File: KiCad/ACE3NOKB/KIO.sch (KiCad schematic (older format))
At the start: 7 parts, among them J100 Conn_02x05_Odd_Even, J101 Conn_02x05_Odd_Even, J102 Conn_02x05_Odd_Even, J103 Conn_02x03_Odd_Even, J104 Conn_02x03_Odd_Even, J105 Conn_02x04_Odd_Even

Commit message: Double check transistors
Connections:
- net ~CPUCLK renamed PHI
- no-connect marks 10 -> 9
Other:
- moved on the sheet: J103, J104, J105
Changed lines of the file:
@@
 	1    0    0    -1
 $EndComp
-NoConn ~ 1350 2850
-NoConn ~ 2575 5950
-Text Label 2475 5650 2    50   ~ 0
+NoConn ~ 2300 5950
+Text Label 2200 5650 2    50   ~ 0
 CLK\TRG0
-Text Label 2475 5750 2    50   ~ 0
+Text Label 2200 5750 2    50   ~ 0
 CLK\TRG1
-Text Label 2475 5850 2    50   ~ 0
+Text Label 2200 5850 2    50   ~ 0
 CLK\TRG2
 $Comp
 L Connector_Generic:Conn_02x04_Odd_Even J105
 U 1 1 6602BBD4
-P 2775 5750
-F 0 "J105" H 2825 6100 50  0000 C CNN
-F 1 "Conn_02x04_Odd_Even" H 2825 6000 50  0000 C CNN
-F 2 "Connector_PinHeader_2.54mm:PinHeader_2x04_P2.54mm_Vertical" H 2775 5750 50  0001 C CNN
-F 3 "~" H 2775 5750 50  0001 C CNN
-	1    2775 5750
+P 2500 5750
+F 0 "J105" H 2550 6100 50  0000 C CNN
+F 1 "Conn_02x04_Odd_Even" H 2550 6000 50  0000 C CNN
+F 2 "Connector_PinHeader_2.54mm:PinHeader_2x04_P2.54mm_Vertical" H 2500 5750 50  0001 C CNN
+F 3 "~" H 2500 5750 50  0001 C CNN
+	1    2500 5750
 	1    0    0    -1
 $EndComp
@@
 L Connector_Generic:Conn_02x03_Odd_Even J104
 U 1 1 64A32B0F
-P 2775 5150
-F 0 "J104" H 2825 5500 50  0000 C CNN
-F 1 "Conn_02x03_Odd_Even" H 2825 5400 50  0000 C CNN
-F 2 "Connector_PinHeader_2.54mm:PinHeader_2x03_P2.54mm_Vertical" H 2775 5150 50  0001 C CNN
-F 3 "~" H 2775 5150 50  0001 C CNN
-	1    2775 5150
+P 2500 5150
+F 0 "J104" H 2550 5500 50  0000 C CNN
+F 1 "Conn_02x03_Odd_Even" H 2550 5400 50  0000 C CNN
+F 2 "Connector_PinHeader_2.54mm:PinHeader_2x03_P2.54mm_Vertical" H 2500 5150 50  0001 C CNN
+F 3 "~" H 2500 5150 50  0001 C CNN
+	1    2500 5150
 	1    0    0    -1
 $EndComp
@@
 L Connector_Generic:Conn_02x03_Odd_Even J103
 U 1 1 6454B474
-P 2775 4550
-F 0 "J103" H 2850 4900 50  0000 C CNN
-F 1 "Conn_02x03_Odd_Even" H 2850 4800 50  0000 C CNN
-F 2 "Connector_PinHeader_2.54mm:PinHeader_2x03_P2.54mm_Vertical" H 2775 4550 50  0001 C CNN
-F 3 "~" H 2775 4550 50  0001 C CNN
-	1    2775 4550
-	1    0    0    -1
-$EndComp
-Text Label 3175 5950 0    50   ~ 0
+P 2500 4550
+F 0 "J103" H 2575 4900 50  0000 C CNN
+F 1 "Conn_02x03_Odd_Even" H 2575 4800 50  0000 C CNN
+F 2 "Connector_PinHeader_2.54mm:PinHeader_2x03_P2.54mm_Vertical" H 2500 4550 50  0001 C CNN
+F 3 "~" H 2500 4550 50  0001 C CNN
+	1    2500 4550
+	1    0    0    -1
+$EndComp
+Text Label 2900 5950 0    50   ~ 0
 ZC\TO3
 Wire Wire Line
-	3075 5950 3175 5950
-Text Label 3175 5850 0    50   ~ 0
+	2800 5950 2900 5950
+Text Label 2900 5850 0    50   ~ 0
 ZC\TO2
 Wire Wire Line
-	3075 5850 3175 5850
-Text Label 3175 5750 0    50   ~ 0
+	2800 5850 2900 5850
+Text Label 2900 5750 0    50   ~ 0
 ZC\TO1
 Wire Wire Line
-	3075 5750 3175 5750
-Text Label 3175 5650 0    50   ~ 0
+	2800 5750 2900 5750
+Text Label 2900 5650 0    50   ~ 0
 ZC\TO0
 Wire Wire Line
-	3075 5650 3175 5650
-Wire Wire Line
-	2575 5850 2475 5850
-Wire Wire Line
-	2575 5750 2475 5750
-Wire Wire Line
-	2575 5650 2475 5650
-Text Label 3175 5250 0    50   ~ 0
+	2800 5650 2900 5650
+Wire Wire Line
+	2300 5850 2200 5850
+Wire Wire Line
+	2300 5750 2200 5750
+Wire Wire Line
+	2300 5650 2200 5650
+Text Label 2900 5250 0    50   ~ 0
 ~CTSB
 Wire Wire Line
-	3075 5250 3175 5250
-Text Label 3175 5150 0    50   ~ 0
+	2800 5250 2900 5250
+Text Label 2900 5150 0    50   ~ 0
 ~DCDB
 Wire Wire Line
-	3075 5150 3175 5150
-Text Label 2475 5050 2    50   ~ 0
+	2800 5150 2900 5150
+Text Label 2200 5050 2    50   ~ 0
 TxDB
 Wire Wire Line
-	2575 5050 2475 5050
-Text Label 2475 5150 2    50   ~ 0
+	2300 5050 2200 5050
+Text Label 2200 5150 2    50   ~ 0
 ~TxCB
 Wire Wire Line
-	2575 5150 2475 5150
-Text Label 2475 5250 2    50   ~ 0
+	2300 5150 2200 5150
+Text Label 2200 5250 2    50   ~ 0
 ~RxCB
 Wire Wire Line
-	2575 5250 2475 5250
-Text Label 3175 5050 0    50   ~ 0
+	2300 5250 2200 5250
+Text Label 2900 5050 0    50   ~ 0
 RxDB
 Wire Wire Line
-	3075 5050 3175 5050
-Text Label 3175 4650 0    50   ~ 0
+	2800 5050 2900 5050
+Text Label 2900 4650 0    50   ~ 0
 ~CTSA
 Wire Wire Line
-	3075 4650 3175 4650
-Text Label 3175 4550 0    50   ~ 0
+	2800 4650 2900 4650
+Text Label 2900 4550 0    50   ~ 0
 ~DCDA
 Wire Wire Line
-	3075 4550 3175 4550
-Text Label 3175 4450 0    50   ~ 0
+	2800 4550 2900 4550
+Text Label 2900 4450 0    50   ~ 0
 RxDA
 Wire Wire Line
-	3075 4450 3175 4450
-Text Label 2475 4650 2    50   ~ 0
+	2800 4450 2900 4450
+Text Label 2200 4650 2    50   ~ 0
 ~RxCA
 Wire Wire Line
-	2575 4650 2475 4650
-Text Label 2475 4550 2    50   ~ 0
+	2300 4650 2200 4650
+Text Label 2200 4550 2    50   ~ 0
 ~TxCA
 Wire Wire Line
-	2575 4550 2475 4550
-Text Label 2475 4450 2    50   ~ 0
+	2300 4550 2200 4550
+Text Label 2200 4450 2    50   ~ 0
 TxDA
 Wire Wire Line
-	2575 4450 2475 4450
+	2300 4450 2200 4450
 $Comp
 L Connector_Generic:Conn_02x05_Odd_Even J100
@@
 ZC\TO3
 Text GLabel 8550 4400 2    50   Input ~ 0
-~CPUCLK
+PHI
 $EndSCHEMATC

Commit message: Update with best part numbers. ad DB of TI parts
Signed-off-by: John Bradley <flypie@rocketmail.com>
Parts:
- J100, J101, J102: Manufacturer_Name (none) -> SAMTEC; Manufacturer_Part_Number (none) -> TSW–105–10–T–D–RA
- J103, J104: Manufacturer_Name (none) -> SAMTEC; Manufacturer_Part_Number (none) -> TSW–103–10–T–D–RA
- J105: Manufacturer_Name (none) -> SAMTEC; Manufacturer_Part_Number (none) -> TSW–104–10–T–D–RA
- Z112: Manufacturer_Name (none) -> Zilog; Manufacturer_Part_Number (none) -> Z84C9010VEG
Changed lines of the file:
@@
 F 1 "Z84-KIO-PLCC-84" H 4350 2475 50  0000 L CNN
 F 2 "Package_LCC:PLCC-84_THT-Socket" H 7100 3750 50  0001 C CNN
-F 3 "https://www.mouser.com/datasheet/2/450/ps0118-25896.pdf" H 6400 1250 50  0001 C CNN
+F 3 "" H 6400 1250 50  0001 C CNN
+F 4 "Zilog" H 5250 2350 50  0001 C CNN "Manufacturer_Name"
+F 5 "Z84C9010VEG" H 5250 2350 50  0001 C CNN "Manufacturer_Part_Number"
 	1    5250 2350
 	1    0    0    -1
@@
 F 1 "Conn_02x04_Odd_Even" H 2550 6000 50  0000 C CNN
 F 2 "Connector_PinHeader_2.54mm:PinHeader_2x04_P2.54mm_Vertical" H 2500 5750 50  0001 C CNN
-F 3 "~" H 2500 5750 50  0001 C CNN
+F 3 "" H 2500 5750 50  0001 C CNN
+F 4 "SAMTEC" H 2500 5750 50  0001 C CNN "Manufacturer_Name"
+F 5 "TSW–104–10–T–D–RA" H 2500 5750 50  0001 C CNN "Manufacturer_Part_Number"
 	1    2500 5750
 	1    0    0    -1
@@
 F 1 "Conn_02x03_Odd_Even" H 2550 5400 50  0000 C CNN
 F 2 "Connector_PinHeader_2.54mm:PinHeader_2x03_P2.54mm_Vertical" H 2500 5150 50  0001 C CNN
-F 3 "~" H 2500 5150 50  0001 C CNN
+F 3 "" H 2500 5150 50  0001 C CNN
+F 4 "SAMTEC" H 2500 5150 50  0001 C CNN "Manufacturer_Name"
+F 5 "TSW–103–10–T–D–RA" H 2500 5150 50  0001 C CNN "Manufacturer_Part_Number"
 	1    2500 5150
 	1    0    0    -1
@@
 F 1 "Conn_02x03_Odd_Even" H 2575 4800 50  0000 C CNN
 F 2 "Connector_PinHeader_2.54mm:PinHeader_2x03_P2.54mm_Vertical" H 2500 4550 50  0001 C CNN
-F 3 "~" H 2500 4550 50  0001 C CNN
+F 3 "" H 2500 4550 50  0001 C CNN
+F 4 "SAMTEC" H 2500 4550 50  0001 C CNN "Manufacturer_Name"
+F 5 "TSW–103–10–T–D–RA" H 2500 4550 50  0001 C CNN "Manufacturer_Part_Number"
 	1    2500 4550
 	1    0    0    -1
@@
 F 1 "Conn_02x05_Odd_Even" H 2575 2275 50  0000 C CNN
 F 2 "Connector_PinHeader_2.54mm:PinHeader_2x05_P2.54mm_Vertical" H 2525 1925 50  0001 C CNN
-F 3 "~" H 2525 1925 50  0001 C CNN
+F 3 "" H 2525 1925 50  0001 C CNN
+F 4 "SAMTEC" H 2525 1925 50  0001 C CNN "Manufacturer_Name"
+F 5 "TSW–105–10–T–D–RA" H 2525 1925 50  0001 C CNN "Manufacturer_Part_Number"
 	1    2525 1925
 	1    0    0    -1
@@
 F 1 "Conn_02x05_Odd_Even" H 2575 3075 50  0000 C CNN
 F 2 "Connector_PinHeader_2.54mm:PinHeader_2x05_P2.54mm_Vertical" H 2525 2725 50  0001 C CNN
-F 3 "~" H 2525 2725 50  0001 C CNN
+F 3 "" H 2525 2725 50  0001 C CNN
+F 4 "SAMTEC" H 2525 2725 50  0001 C CNN "Manufacturer_Name"
+F 5 "TSW–105–10–T–D–RA" H 2525 2725 50  0001 C CNN "Manufacturer_Part_Number"
 	1    2525 2725
 	1    0    0    -1
@@
 F 1 "Conn_02x05_Odd_Even" H 2600 3875 50  0000 C CNN
 F 2 "Connector_PinHeader_2.54mm:PinHeader_2x05_P2.54mm_Vertical" H 2525 3525 50  0001 C CNN
-F 3 "~" H 2525 3525 50  0001 C CNN
+F 3 "" H 2525 3525 50  0001 C CNN
+F 4 "SAMTEC" H 2525 3525 50  0001 C CNN "Manufacturer_Name"
+F 5 "TSW–105–10–T–D–RA" H 2525 3525 50  0001 C CNN "Manufacturer_Part_Number"
 	1    2525 3525
 	1    0    0    -1

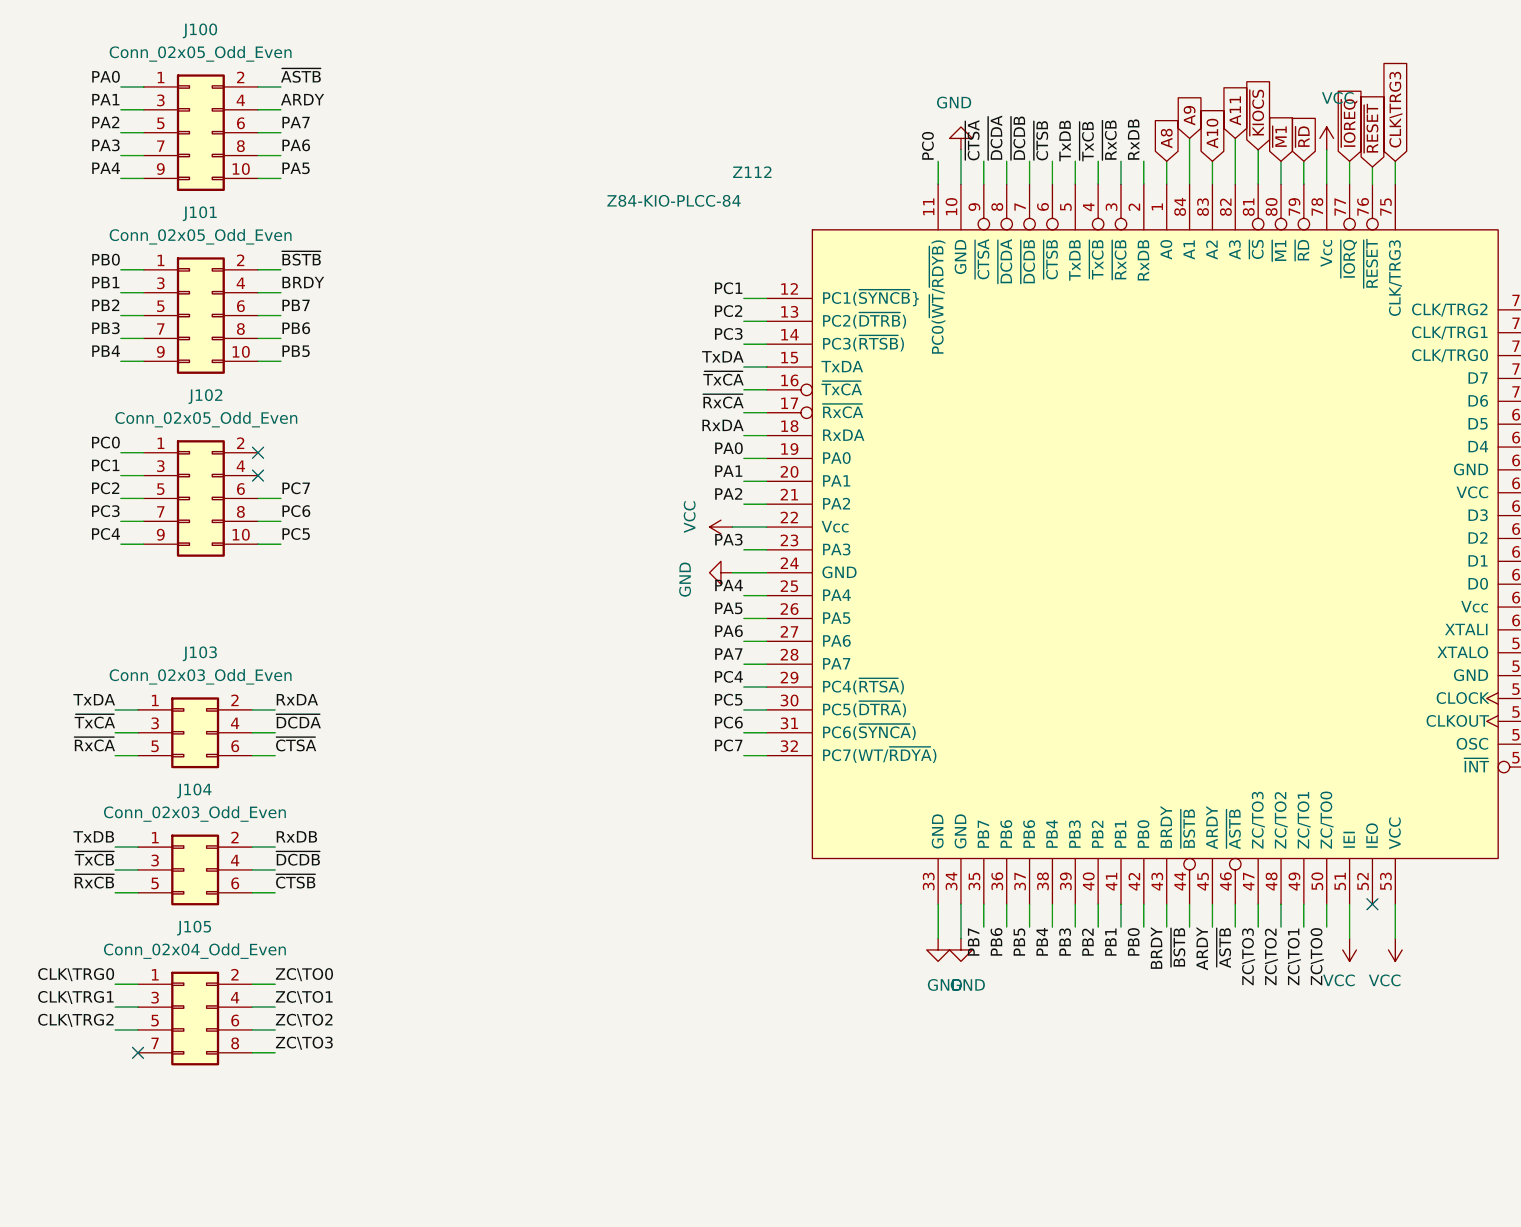
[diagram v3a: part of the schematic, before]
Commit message: Update IO port decoding.
Signed-off-by: John Bradley <flypie@rocketmail.com>
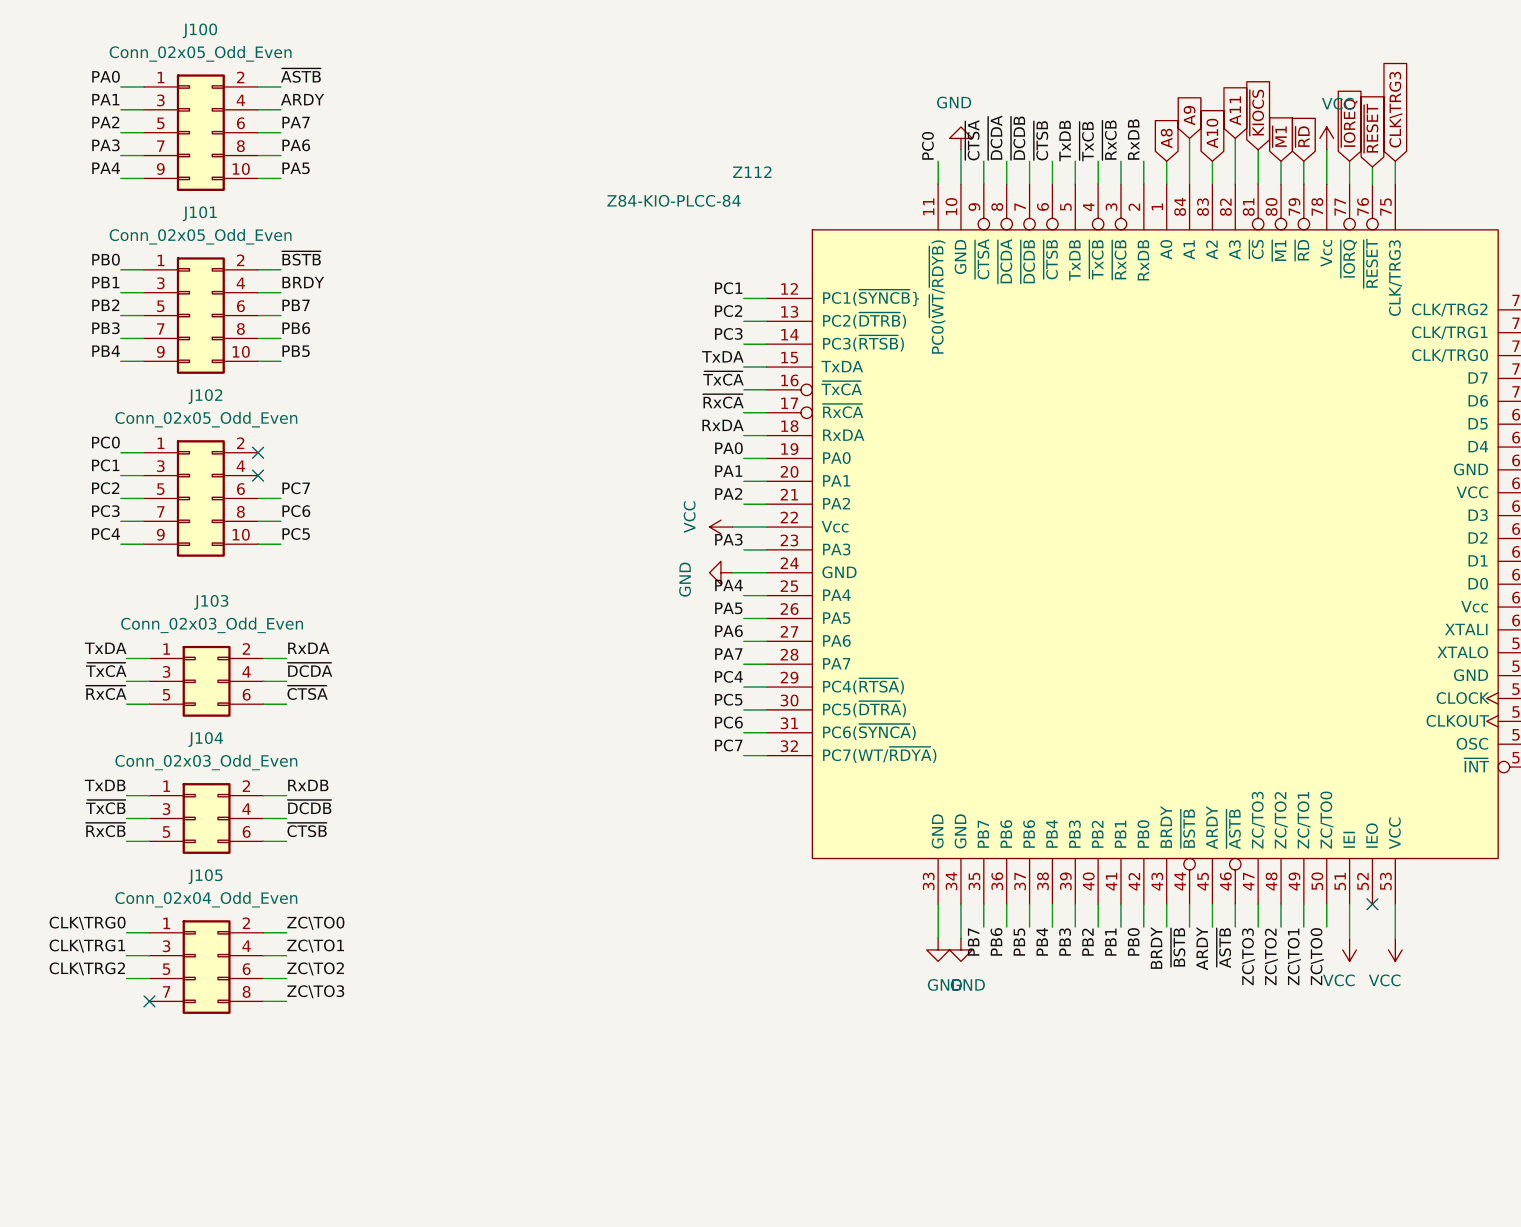
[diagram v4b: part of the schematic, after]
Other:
- moved on the sheet: J103, J104, J105
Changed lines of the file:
@@
 EESchema Schematic File Version 4
 LIBS:ACE3NOKB-cache
+LIBS:temp-cache
 EELAYER 30 0
 EELAYER END
@@
 P 7500 2000
 F 0 "#~PWR0173" H 7500 1850 50  0001 C CNN
-F 1 "VCC" H 7550 2225 50  0000 C CNN
+F 1 "VCC" H 7550 2200 50  0000 C CNN
 F 2 "" H 7500 2000 50  0001 C CNN
 F 3 "" H 7500 2000 50  0001 C CNN
@@
 	1    0    0    -1
 $EndComp
-NoConn ~ 2300 5950
-Text Label 2200 5650 2    50   ~ 0
+NoConn ~ 2350 5725
+Text Label 2250 5425 2    50   ~ 0
 CLK\TRG0
-Text Label 2200 5750 2    50   ~ 0
+Text Label 2250 5525 2    50   ~ 0
 CLK\TRG1
-Text Label 2200 5850 2    50   ~ 0
+Text Label 2250 5625 2    50   ~ 0
 CLK\TRG2
 $Comp
 L Connector_Generic:Conn_02x04_Odd_Even J105
 U 1 1 6602BBD4
-P 2500 5750
-F 0 "J105" H 2550 6100 50  0000 C CNN
-F 1 "Conn_02x04_Odd_Even" H 2550 6000 50  0000 C CNN
-F 2 "Connector_PinHeader_2.54mm:PinHeader_2x04_P2.54mm_Vertical" H 2500 5750 50  0001 C CNN
-F 3 "" H 2500 5750 50  0001 C CNN
-F 4 "SAMTEC" H 2500 5750 50  0001 C CNN "Manufacturer_Name"
-F 5 "TSW–104–10–T–D–RA" H 2500 5750 50  0001 C CNN "Manufacturer_Part_Number"
-	1    2500 5750
+P 2550 5525
+F 0 "J105" H 2600 5875 50  0000 C CNN
+F 1 "Conn_02x04_Odd_Even" H 2600 5775 50  0000 C CNN
+F 2 "Connector_PinHeader_2.54mm:PinHeader_2x04_P2.54mm_Vertical" H 2550 5525 50  0001 C CNN
+F 3 "" H 2550 5525 50  0001 C CNN
+F 4 "SAMTEC" H 2550 5525 50  0001 C CNN "Manufacturer_Name"
+F 5 "TSW–104–10–T–D–RA" H 2550 5525 50  0001 C CNN "Manufacturer_Part_Number"
+	1    2550 5525
 	1    0    0    -1
 $EndComp
@@
 L Connector_Generic:Conn_02x03_Odd_Even J104
 U 1 1 64A32B0F
-P 2500 5150
-F 0 "J104" H 2550 5500 50  0000 C CNN
-F 1 "Conn_02x03_Odd_Even" H 2550 5400 50  0000 C CNN
-F 2 "Connector_PinHeader_2.54mm:PinHeader_2x03_P2.54mm_Vertical" H 2500 5150 50  0001 C CNN
-F 3 "" H 2500 5150 50  0001 C CNN
-F 4 "SAMTEC" H 2500 5150 50  0001 C CNN "Manufacturer_Name"
-F 5 "TSW–103–10–T–D–RA" H 2500 5150 50  0001 C CNN "Manufacturer_Part_Number"
-	1    2500 5150
+P 2550 4925
+F 0 "J104" H 2600 5275 50  0000 C CNN
+F 1 "Conn_02x03_Odd_Even" H 2600 5175 50  0000 C CNN
+F 2 "Connector_PinHeader_2.54mm:PinHeader_2x03_P2.54mm_Vertical" H 2550 4925 50  0001 C CNN
+F 3 "" H 2550 4925 50  0001 C CNN
+F 4 "SAMTEC" H 2550 4925 50  0001 C CNN "Manufacturer_Name"
+F 5 "TSW–103–10–T–D–RA" H 2550 4925 50  0001 C CNN "Manufacturer_Part_Number"
+	1    2550 4925
 	1    0    0    -1
 $EndComp
@@
 L Connector_Generic:Conn_02x03_Odd_Even J103
 U 1 1 6454B474
-P 2500 4550
-F 0 "J103" H 2575 4900 50  0000 C CNN
-F 1 "Conn_02x03_Odd_Even" H 2575 4800 50  0000 C CNN
-F 2 "Connector_PinHeader_2.54mm:PinHeader_2x03_P2.54mm_Vertical" H 2500 4550 50  0001 C CNN
-F 3 "" H 2500 4550 50  0001 C CNN
-F 4 "SAMTEC" H 2500 4550 50  0001 C CNN "Manufacturer_Name"
-F 5 "TSW–103–10–T–D–RA" H 2500 4550 50  0001 C CNN "Manufacturer_Part_Number"
-	1    2500 4550
-	1    0    0    -1
-$EndComp
-Text Label 2900 5950 0    50   ~ 0
+P 2550 4325
+F 0 "J103" H 2625 4675 50  0000 C CNN
+F 1 "Conn_02x03_Odd_Even" H 2625 4575 50  0000 C CNN
+F 2 "Connector_PinHeader_2.54mm:PinHeader_2x03_P2.54mm_Vertical" H 2550 4325 50  0001 C CNN
+F 3 "" H 2550 4325 50  0001 C CNN
+F 4 "SAMTEC" H 2550 4325 50  0001 C CNN "Manufacturer_Name"
+F 5 "TSW–103–10–T–D–RA" H 2550 4325 50  0001 C CNN "Manufacturer_Part_Number"
+	1    2550 4325
+	1    0    0    -1
+$EndComp
+Text Label 2950 5725 0    50   ~ 0
 ZC\TO3
 Wire Wire Line
-	2800 5950 2900 5950
-Text Label 2900 5850 0    50   ~ 0
+	2850 5725 2950 5725
+Text Label 2950 5625 0    50   ~ 0
 ZC\TO2
 Wire Wire Line
-	2800 5850 2900 5850
-Text Label 2900 5750 0    50   ~ 0
+	2850 5625 2950 5625
+Text Label 2950 5525 0    50   ~ 0
 ZC\TO1
 Wire Wire Line
-	2800 5750 2900 5750
-Text Label 2900 5650 0    50   ~ 0
+	2850 5525 2950 5525
+Text Label 2950 5425 0    50   ~ 0
 ZC\TO0
 Wire Wire Line
-	2800 5650 2900 5650
-Wire Wire Line
-	2300 5850 2200 5850
-Wire Wire Line
-	2300 5750 2200 5750
-Wire Wire Line
-	2300 5650 2200 5650
-Text Label 2900 5250 0    50   ~ 0
+	2850 5425 2950 5425
+Wire Wire Line
+	2350 5625 2250 5625
+Wire Wire Line
+	2350 5525 2250 5525
+Wire Wire Line
+	2350 5425 2250 5425
+Text Label 2950 5025 0    50   ~ 0
 ~CTSB
 Wire Wire Line
-	2800 5250 2900 5250
-Text Label 2900 5150 0    50   ~ 0
+	2850 5025 2950 5025
+Text Label 2950 4925 0    50   ~ 0
 ~DCDB
 Wire Wire Line
-	2800 5150 2900 5150
-Text Label 2200 5050 2    50   ~ 0
+	2850 4925 2950 4925
+Text Label 2250 4825 2    50   ~ 0
 TxDB
 Wire Wire Line
-	2300 5050 2200 5050
-Text Label 2200 5150 2    50   ~ 0
+	2350 4825 2250 4825
+Text Label 2250 4925 2    50   ~ 0
 ~TxCB
 Wire Wire Line
-	2300 5150 2200 5150
-Text Label 2200 5250 2    50   ~ 0
+	2350 4925 2250 4925
+Text Label 2250 5025 2    50   ~ 0
 ~RxCB
 Wire Wire Line
-	2300 5250 2200 5250
-Text Label 2900 5050 0    50   ~ 0
+	2350 5025 2250 5025
+Text Label 2950 4825 0    50   ~ 0
 RxDB
 Wire Wire Line
-	2800 5050 2900 5050
-Text Label 2900 4650 0    50   ~ 0
+	2850 4825 2950 4825
+Text Label 2950 4425 0    50   ~ 0
 ~CTSA
 Wire Wire Line
-	2800 4650 2900 4650
-Text Label 2900 4550 0    50   ~ 0
+	2850 4425 2950 4425
+Text Label 2950 4325 0    50   ~ 0
 ~DCDA
 Wire Wire Line
-	2800 4550 2900 4550
-Text Label 2900 4450 0    50   ~ 0
+	2850 4325 2950 4325
+Text Label 2950 4225 0    50   ~ 0
 RxDA
 Wire Wire Line
-	2800 4450 2900 4450
-Text Label 2200 4650 2    50   ~ 0
+	2850 4225 2950 4225
+Text Label 2250 4425 2    50   ~ 0
 ~RxCA
 Wire Wire Line
-	2300 4650 2200 4650
-Text Label 2200 4550 2    50   ~ 0
+	2350 4425 2250 4425
+Text Label 2250 4325 2    50   ~ 0
 ~TxCA
 Wire Wire Line
-	2300 4550 2200 4550
-Text Label 2200 4450 2    50   ~ 0
+	2350 4325 2250 4325
+Text Label 2250 4225 2    50   ~ 0
 TxDA
 Wire Wire Line
-	2300 4450 2200 4450
+	2350 4225 2250 4225
 $Comp
 L Connector_Generic:Conn_02x05_Odd_Even J100
